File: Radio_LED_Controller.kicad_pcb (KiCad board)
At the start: 2 copper layers, 21.5 x 12.5 mm, 17 parts, among them J1 Conn_01x04_Pin, J2 Conn_01x03_Pin, J3 Conn_01x05, J4 UPDI, J5 Conn_01x02_Pin, J6 Conn_01x02_Pin, J7 Conn_01x05, J8 Conn_01x03_Pin, J9 Conn_01x03_Pin, Q2 SS8050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

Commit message: v0.2
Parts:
- J2: moved to B.Cu
- J3, J7: footprint Connector_JST:JST_GH_SM05B-GHS-TB_1x05-1MP_P1.25mm_Horizontal -> Connector_Molex:Molex_PicoBlade_53261-0571_1x05-1MP_P1.25mm_Horizontal
- moved J2 22.7 mm to (185.9, 88.7)
- moved Q3 7.73 mm to (181.8, 93.1), turned to 0 degrees
- moved R3 5.29 mm to (181.5, 90.7), turned to 0 degrees
- moved J4 4.48 mm to (177.4, 93.5)
- moved G*** 3.99 mm to (177.3, 90.2)
- moved U1 3.87 mm to (174.4, 92.0)
- moved C2 3.29 mm to (178.2, 91.5), turned to 0 degrees
- moved J1 3.14 mm to (167.7, 92.8), turned to 180 degrees
- moved J8 2.70 mm to (169.1, 85.4)
- moved G*** 2.57 mm to (172.7, 89.2)
- moved J3 2.49 mm to (166.1, 86.2)
- moved R2 2.38 mm to (170.4, 90.7), turned to 180 degrees
- moved J6 2.20 mm to (185.1, 93.0), turned to 90 degrees
- moved J5 1.82 mm to (165.8, 90.8), turned to 180 degrees
- moved Q2 1.39 mm to (170.2, 93.1), turned to 180 degrees
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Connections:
- J3 pad 1: Net-(J3-Pin_1) -> GND
- J3 pad 2: unconnected-(J3-Pin_2-Pad2) -> RGB1
- J3 pad 4: RGB1 -> unconnected-(J3-Pin_4-Pad4)
- J3 pad 5: GND -> Net-(J3-Pin_5)
- J5 pad 1: Net-(J3-Pin_1) -> Net-(J3-Pin_5)
- J7 pad 1: Net-(J6-Pin_1) -> GND
- J7 pad 2: unconnected-(J7-Pin_2-Pad2) -> RGB2
- J7 pad 4: RGB2 -> unconnected-(J7-Pin_4-Pad4)
- J7 pad 5: GND -> Net-(J6-Pin_1)
- Q2 pad 3: Net-(J3-Pin_1) -> Net-(J3-Pin_5)
- U1 pad 13: LED2 -> LED1
- U1 pad 14: LED1 -> LED2
- U1 pad 2: RGB1 -> RGB3
- U1 pad 6: RGB3 -> RGB1
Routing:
- net GND: track 58.0 -> 69.1 mm, vias 7 -> 5
- net LED1: track 12.3 -> 2.30 mm, vias 2 -> 0
- net Net-(J3-Pin_1): track 8.04 -> 0.00 mm
- net Net-(J3-Pin_5): track 0.00 -> 7.94 mm
- net RGB3: track 17.2 -> 9.65 mm, vias 2 -> 1
- net RGB1: track 21.5 -> 14.2 mm, vias 3 -> 1
- net RGB2: track 7.83 -> 12.1 mm
- net LED2: track 6.56 -> 10.4 mm, vias 0 -> 2
- net Net-(Q3-B): track 5.62 -> 2.21 mm
- net Net-(J6-Pin_1): track 14.6 -> 11.6 mm, vias 0 -> 2
- net Tx: track 8.29 -> 11.2 mm
- net Net-(Q2-B): track 1.65 -> 4.06 mm
- net Rx: track 10.5 -> 8.10 mm, vias 0 -> 2
- net VCC: track 50.9 -> 48.9 mm, vias 4 -> 3
- net Net-(J4-Pin_1): track 3.98 -> 3.39 mm
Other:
- board size 21.5 x 12.5 mm -> 26.4 x 11.5 mm
- board text added: "${SCHEMATIC_VERSION}"
- board text added: "JLCJLCJLCJLC"
- board text added: "^"

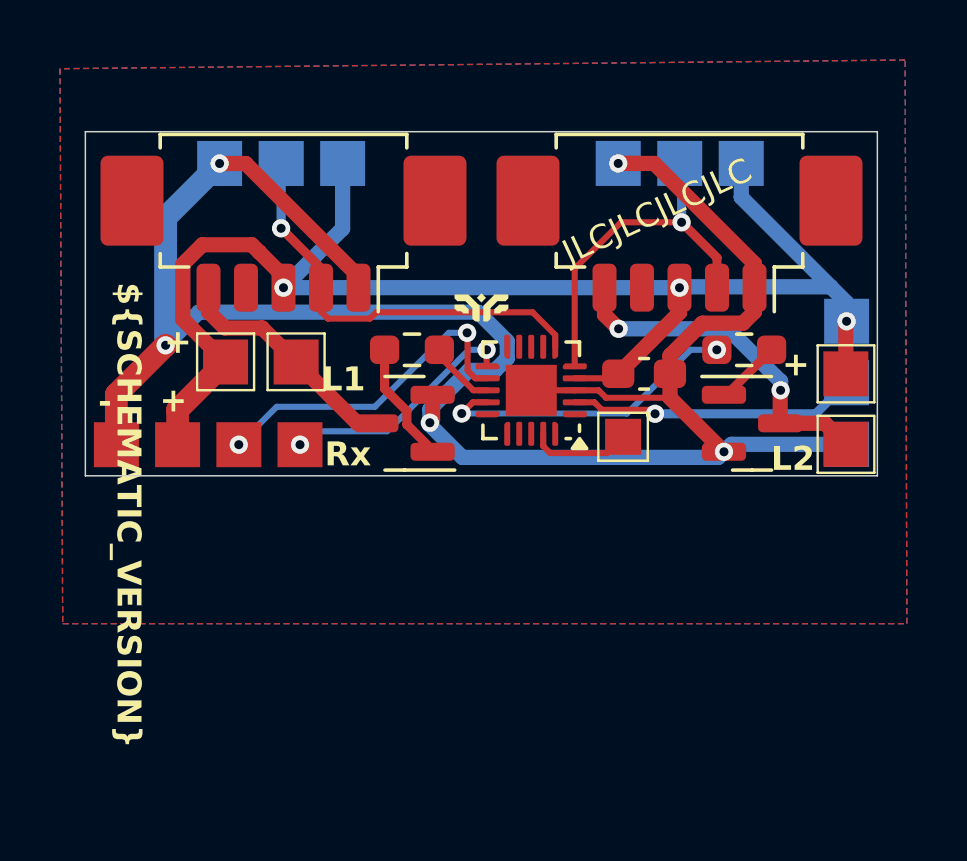
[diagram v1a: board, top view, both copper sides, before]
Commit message: v0.3 - vias for stronger pads
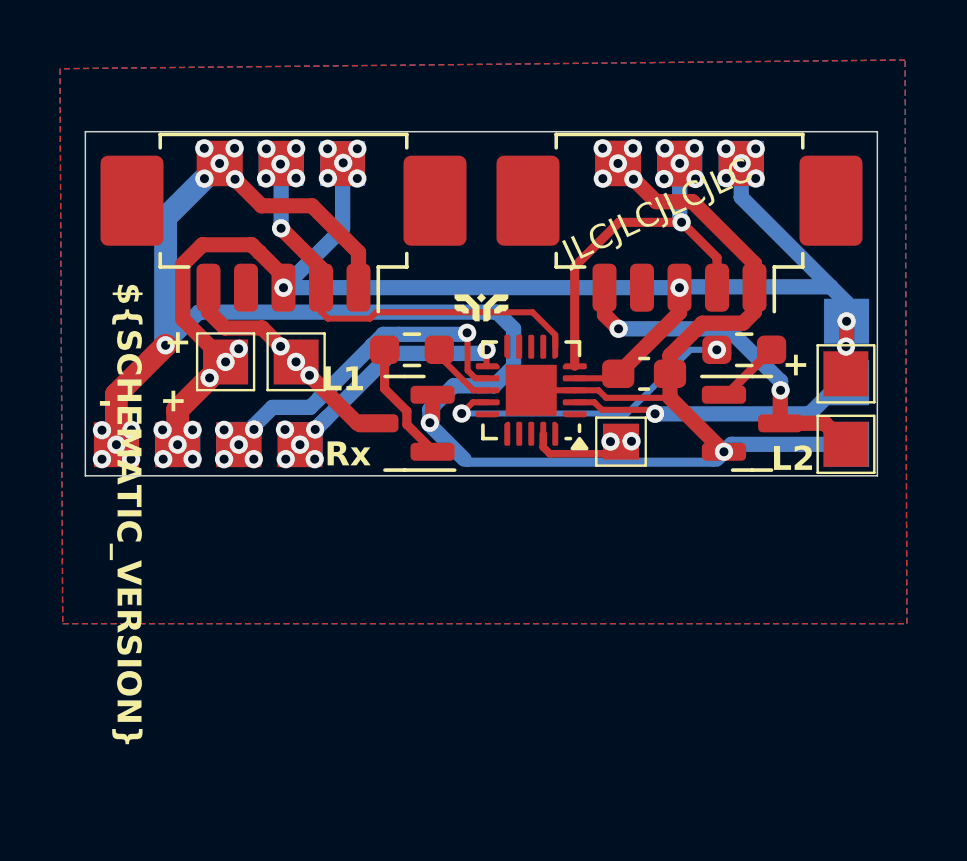
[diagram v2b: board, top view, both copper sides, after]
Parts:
- moved J4 0.17 mm to (177.4, 93.7)
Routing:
- net VCC: track 48.9 -> 73.4 mm, vias 3 -> 22
- net GND: track 69.1 -> 89.7 mm, vias 5 -> 18
- net RGB1: track 14.2 -> 23.1 mm, vias 1 -> 6
- net RGB2: track 12.1 -> 19.1 mm, vias 1 -> 6
- net Rx: track 8.10 -> 14.7 mm, vias 2 -> 6
- net Tx: track 11.2 -> 17.3 mm, vias 2 -> 6
- net Net-(J4-Pin_1): track 3.39 -> 4.70 mm, vias 0 -> 2
- net Net-(J3-Pin_5): track 7.94 -> 8.57 mm, vias 0 -> 3
